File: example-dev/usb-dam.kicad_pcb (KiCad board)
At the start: 2 copper layers, 44 parts, among them J1 USB_C_Receptacle, J2 Conn_01x08_Pin, U1 MCP6002-xMC, U2 SiP32431DR3, U3 TMUX1574RSVR, U4 74LVC1G08

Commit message: layout example board
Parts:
- removed TP1, TP10, TP11, TP6, TP9: TestPoint, tuna-f1sh/jbr-kicad/Misc.pretty:TestPoint_Pad_D1.0mm_Tight
- added G***: LOGO, tuna-f1sh/jbr-kicad/Logos.pretty:jbr-binary-xs-mask, F.Cu at (131.4, 80.7)
- TP5: moved to B.Cu
- moved J1 48.6 mm to (110.5, 90.5), turned to -90 degrees
- moved D1 41.9 mm to (120.3, 96.5), turned to -90 degrees
- moved TP13 37.9 mm to (123.2, 86.3)
- moved U2 37.5 mm to (126.5, 91.7)
- moved FB1 37.4 mm to (109.7, 81.5)
- moved TP12 37.2 mm to (123.8, 84.3)
- moved R1 36.7 mm to (111.3, 97.7)
- moved JP4 36.6 mm to (125.7, 99.2), turned to 180 degrees
- moved TP7 34.6 mm to (122.3, 91.9)
- moved TP8 34.6 mm to (122.3, 94.3)
- moved FB3 34.3 mm to (114.5, 97.7), turned to 180 degrees
- moved C1 33.4 mm to (109.7, 83.0)
- moved FB2 32.6 mm to (114.6, 83.0), turned to 180 degrees
- moved C4 31.7 mm to (112.2, 82.2), turned to 90 degrees
- moved R7 31.0 mm to (120.2, 87.8), turned to 180 degrees
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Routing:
- net VBUS: track 0.00 -> 47.4 mm, vias 0 -> 2
- net VCC: track 0.00 -> 47.2 mm, vias 0 -> 7
- net /RX+: track 0.00 -> 35.3 mm, vias 0 -> 4
- net /RX-: track 0.00 -> 34.5 mm, vias 0 -> 4
- net /VBUS_CONN: track 0.00 -> 32.2 mm, vias 0 -> 2
- net /TX-: track 0.00 -> 31.0 mm, vias 0 -> 4
- net /TX+: track 0.00 -> 30.3 mm, vias 0 -> 4
- net /SHIELD: track 0.00 -> 29.2 mm
- net /USB_GND: track 0.00 -> 26.9 mm, vias 0 -> 2
- net /SWDIO: track 0.00 -> 22.5 mm, vias 0 -> 2
- net /SWDCLK: track 0.00 -> 20.6 mm, vias 0 -> 1
- net /CC1: track 0.00 -> 19.9 mm
- net /DAM_EN: track 0.00 -> 19.6 mm, vias 0 -> 4
- net /SBU: track 0.00 -> 19.6 mm, vias 0 -> 4
- net Net-(J1-CC2): track 0.00 -> 18.8 mm, vias 0 -> 2
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- added copper zone on B.Cu, net GND
- added copper zone on F.Cu, net GND
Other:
- board outline added: 39 x 25 mm
- board text added: "GND"
- board text added: "RX+"
- board text added: "RX-"
- board text added: "SWDCLK"
- board text added: "SWDIO"
- board text added: "USB DAM Test Board R${REVISION}"
- board text added: "VBUS"
- board text added: "VCC"
- board text added: "~{EN}"

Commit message: example board for production
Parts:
- added TP1: TestPoint, TestPoint:TestPoint_Pad_D2.0mm, F.Cu at (120.8, 99.6)
- added TP6: TestPoint, TestPoint:TestPoint_Pad_D2.0mm, F.Cu at (117.6, 99.5)
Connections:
- net /DAM_RX+ renamed /SWDO/TXD
- net /DAM_RX- renamed /~{NRST}/RXD
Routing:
- net /USB_D+: track 14.9 -> 18.1 mm
- net /USB_D-: track 11.9 -> 14.6 mm

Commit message: README started
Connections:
- net /SWDCLK renamed /SWCLK
- net /SWDO/TXD renamed /SWO/TXD
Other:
- board text added: "SWCLK"
- board text removed: "SWDCLK"

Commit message: pcb render
active layers
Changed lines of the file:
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@@
   (segment (start 117.007107 88) (end 117.65 88.642893) (width 0.2) (layer "F.Cu") (net 9))
   (segment (start 124.05 90.65) (end 124.2 90.5) (width 0.2) (layer "F.Cu") (net 9))
-  (segment (start 112.4 92.149503) (end 112.4 92.207107) (width 0.2) (layer "F.Cu") (net 9))
   (segment (start 129.65 92.6) (end 129.65 93.493393) (width 0.2) (layer "F.Cu") (net 9))
   (segment (start 116.55 88.25) (end 115.57 88.25) (width 0.2) (layer "F.Cu") (net 9))
-  (segment (start 112.4 92.207107) (end 112.692893 92.5) (width 0.2) (layer "F.Cu") (net 9))
+  (segment (start 112.250497 92) (end 112.250497 92.057604) (width 0.2) (layer "F.Cu") (net 9))
+  (segment (start 112.692893 92.5) (end 113.87 92.5) (width 0.2) (layer "F.Cu") (net 9))
   (segment (start 130.206607 94.05) (end 130.85 94.05) (width 0.2) (layer "F.Cu") (net 9))
+  (segment (start 112.250497 92.057604) (end 112.692893 92.5) (width 0.2) (layer "F.Cu") (net 9))
   (segment (start 129.65 93.493393) (end 129.656607 93.5) (width 0.2) (layer "F.Cu") (net 9))
   (segment (start 129.656607 93.5) (end 130.206607 94.05) (width 0.2) (layer "F.Cu") (net 9))
-  (segment (start 112.250497 92) (end 112.4 92.149503) (width 0.2) (layer "F.Cu") (net 9))
   (segment (start 117.65 88.642893) (end 117.65 89.905026) (width 0.2) (layer "F.Cu") (net 9))
   (segment (start 116.8 88) (end 117.007107 88) (width 0.2) (layer "F.Cu") (net 9))
-  (segment (start 112.692893 92.5) (end 113.87 92.5) (width 0.2) (layer "F.Cu") (net 9))
   (via (at 112.250497 92) (size 0.5) (drill 0.3) (layers "F.Cu" "B.Cu") (net 9))
   (via (at 124.2 90.5) (size 0.5) (drill 0.3) (layers "F.Cu" "B.Cu") (net 9))

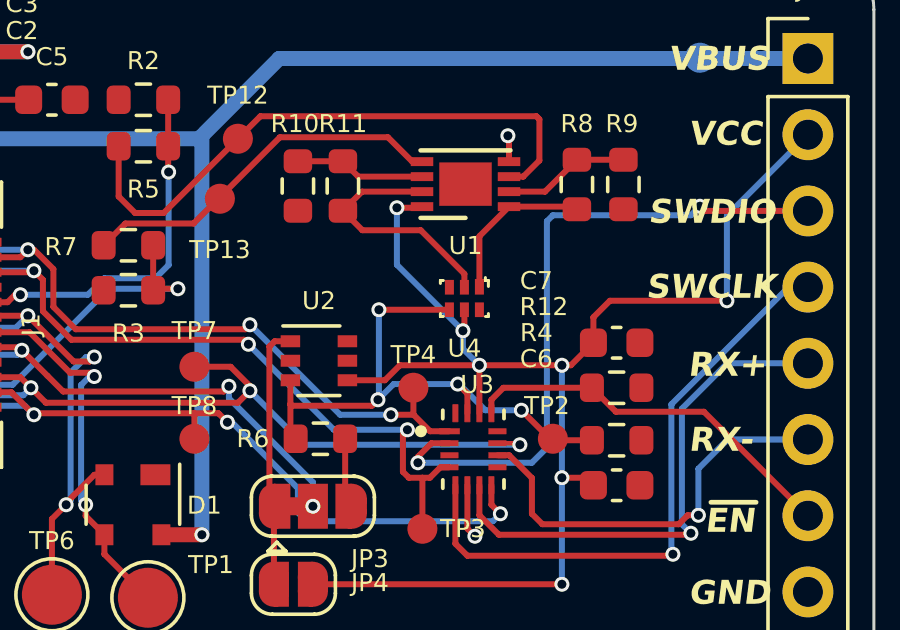
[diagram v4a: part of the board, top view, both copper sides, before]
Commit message: fix example AND footprint VCC 5->6
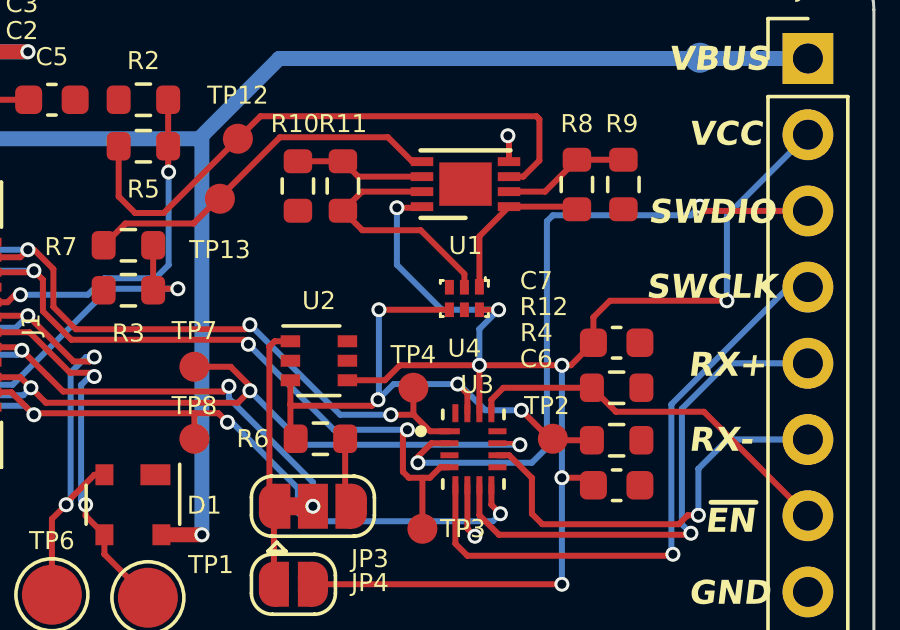
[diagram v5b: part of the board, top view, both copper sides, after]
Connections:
- U4 pad 5: VCC -> (no net)
- U4 pad 6: (no net) -> VCC
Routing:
- net VCC: track 47.2 -> 48.8 mm
